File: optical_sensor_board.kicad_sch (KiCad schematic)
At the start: 18 parts, among them J2 Conn_01x09_Socket, U1 PMW3389DM‐T3QU, U3 LM317L_SOT-89

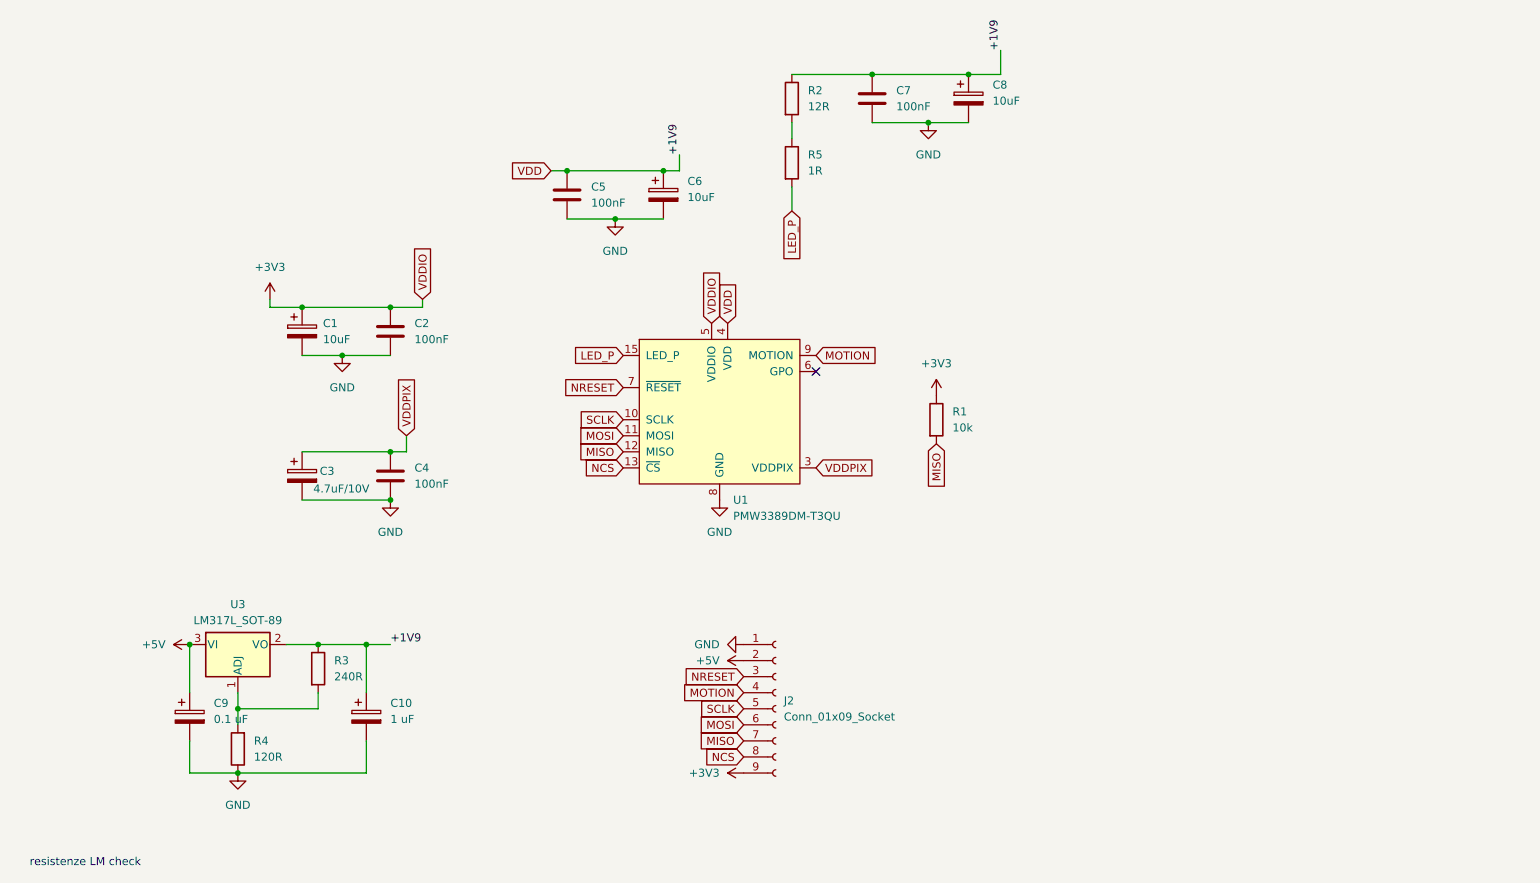
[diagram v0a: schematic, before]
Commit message: Aggiunta copper-area + modifiche a schematico e master
Design:
 - Spostate le tracce sul bottom e i ponti sul top layer
 - Aggiunta la Copper Area sul bottom layer
 - Sistemate le serigrafie

Schematico:
 - Corretti gli errori del ERC aggiungendo i PWR_FLAG
 - Spostati i componenti per far si che si veda almeno un pezzettino di filo

Progetto:
 - Aggiunta la libreria dei footprint
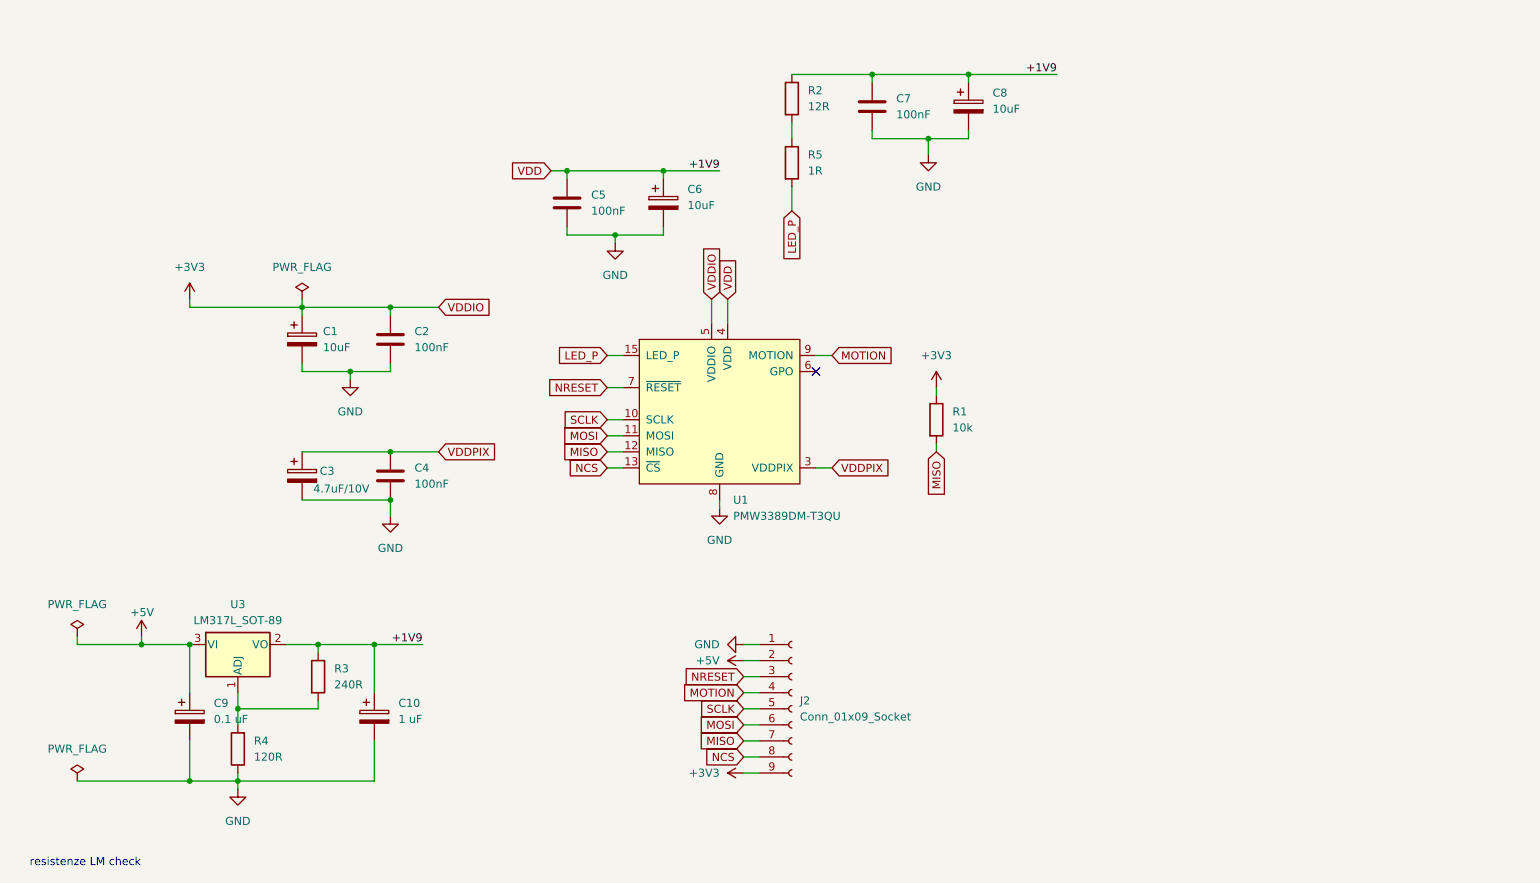
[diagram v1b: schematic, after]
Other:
- moved on the sheet: C1, C10, C2, C5, C6, C7, C8, J2, R3

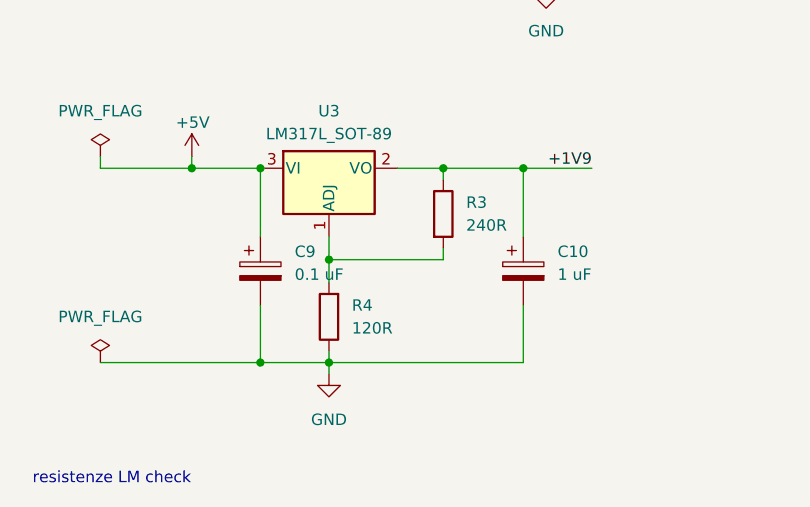
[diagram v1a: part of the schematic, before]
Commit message: add potentiometer in LM317 circuit
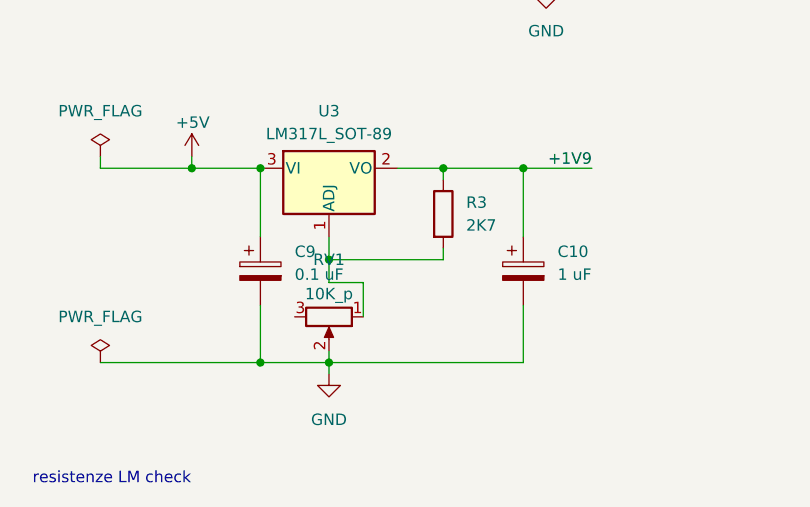
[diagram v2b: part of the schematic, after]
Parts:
- removed R4: 120R, MyOptical:LargePad_R_Axial_DIN0207_L6.3mm_D2.5mm_P10.16mm_Horizontal, symbol Device:R
- added RV1: 10K_p, symbol Device:R_Potentiometer
- R3: value 240R -> 2K7
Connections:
- net GND: now also RV1.2
- net at R3.2, U3.1 (ADJ): now also RV1.1
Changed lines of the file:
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@@
+	(wire
+		(pts
+			(xy 72.39 148.59) (xy 72.39 144.78)
+		)
+		(stroke
+			(width 0)
+			(type default)
+		)
+	)
 	(wire
 		(pts
@@
 		(pts
 			(xy 68.58 142.24) (xy 68.58 144.78)
+		)
+		(stroke
+			(width 0)
+			(type default)
+		)
+	)
+	(wire
+		(pts
+			(xy 72.39 144.78) (xy 68.58 144.78)
 		)
 		(stroke
@@
 	)
 	(symbol
+		(lib_id "Device:R_Potentiometer")
+		(at 68.58 148.59 270)
+		(unit 1)
+		(exclude_from_sim no)
+		(in_bom yes)
+		(on_board yes)
+		(dnp no)
+		(property "Reference" "RV1"
+			(at 68.58 142.24 90)
+			(effects
+				(font
+					(size 1.27 1.27)
+				)
+			)
+		)
+		(property "Value" "10K_p"
+			(at 68.58 146.05 90)
+			(effects
+				(font
+					(size 1.27 1.27)
+				)
+			)
+		)
+		(property "Footprint" ""
+			(at 68.58 148.59 0)
+			(effects
+				(font
+					(size 1.27 1.27)
+				)
+				(hide yes)
+			)
+		)
+		(property "Datasheet" "~"
+			(at 68.58 148.59 0)
+			(effects
+				(font
+					(size 1.27 1.27)
+				)
+				(hide yes)
+			)
+		)
+		(property "Description" "Potentiometer"
+			(at 68.58 148.59 0)
+			(effects
+				(font
+					(size 1.27 1.27)
+				)
+				(hide yes)
+			)
+		)
+		(pin "2"
+		)
+		(pin "1"
+		)
+		(pin "3"
+		)
+		(instances
+			(project ""
+				(path "/bc898632-37cb-47d1-8655-c4a22efc7ca2"
+					(reference "RV1")
+					(unit 1)
+				)
+			)
+		)
+	)
+	(symbol
 		(lib_id "power:GND")
 		(at 177.8 54.61 0)
@@
 				(path "/bc898632-37cb-47d1-8655-c4a22efc7ca2"
 					(reference "#PWR07")
-					(unit 1)
-				)
-			)
-		)
-	)
-	(symbol
-		(lib_id "Device:R")
-		(at 68.58 148.59 180)
-		(unit 1)
-		(exclude_from_sim no)
-		(in_bom yes)
-		(on_board yes)
-		(dnp no)
-		(fields_autoplaced yes)
-		(property "Reference" "R4"
-			(at 71.12 147.3199 0)
-			(effects
-				(font
-					(size 1.27 1.27)
-				)
-				(justify right)
-			)
-		)
-		(property "Value" "120R"
-			(at 71.12 149.8599 0)
-			(effects
-				(font
-					(size 1.27 1.27)
-				)
-				(justify right)
-			)
-		)
-		(property "Footprint" "MyOptical:LargePad_R_Axial_DIN0207_L6.3mm_D2.5mm_P10.16mm_Horizontal"
-			(at 70.358 148.59 90)
-			(effects
-				(font
-					(size 1.27 1.27)
-				)
-				(hide yes)
-			)
-		)
-		(property "Datasheet" "~"
-			(at 68.58 148.59 0)
-			(effects
-				(font
-					(size 1.27 1.27)
-				)
-				(hide yes)
-			)
-		)
-		(property "Description" "Resistor"
-			(at 68.58 148.59 0)
-			(effects
-				(font
-					(size 1.27 1.27)
-				)
-				(hide yes)
-			)
-		)
-		(pin "1"
-		)
-		(pin "2"
-		)
-		(instances
-			(project ""
-				(path "/bc898632-37cb-47d1-8655-c4a22efc7ca2"
-					(reference "R4")
 					(unit 1)
 				)
@@
 			)
 		)
-		(property "Value" "240R"
+		(property "Value" "2K7"
 			(at 83.82 138.4299 0)
 			(effects

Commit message: potentiometer footprint + potentiometer routing
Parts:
- RV1: footprint (none) -> MyOptical:LargerPad_P160
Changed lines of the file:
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@@
 			)
 		)
-		(property "Footprint" ""
+		(property "Footprint" "MyOptical:LargerPad_P160"
 			(at 68.58 148.59 0)
 			(effects

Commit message: copper area
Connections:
- no-connect marks 1 -> 2
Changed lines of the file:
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@@
+	)
+	(no_connect
+		(at 64.77 148.59)
 	)
 	(no_connect

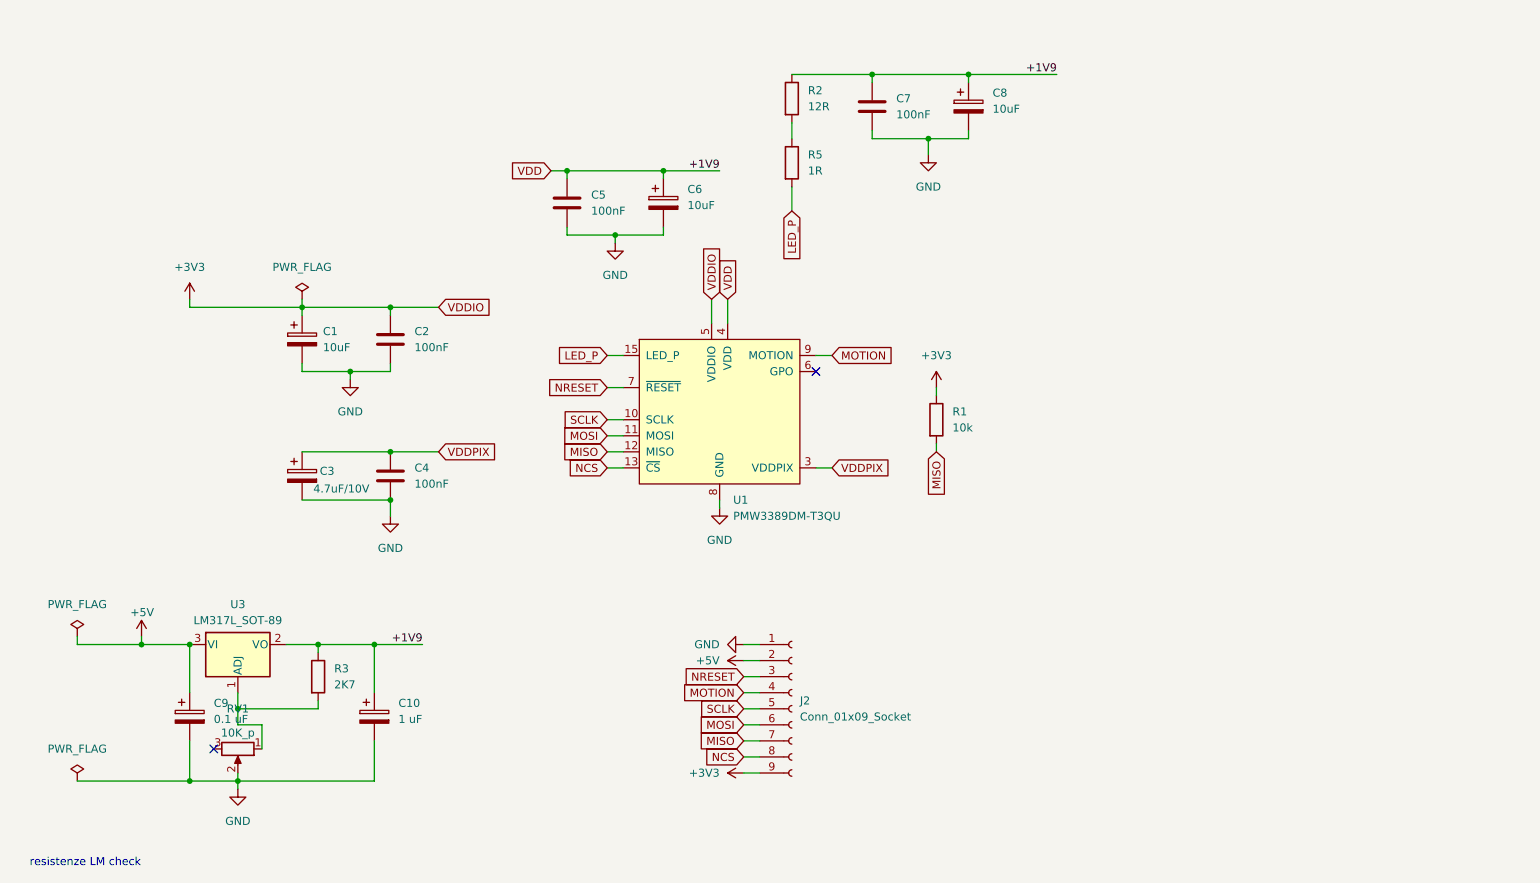
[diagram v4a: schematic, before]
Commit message: TestPoint in Schematic
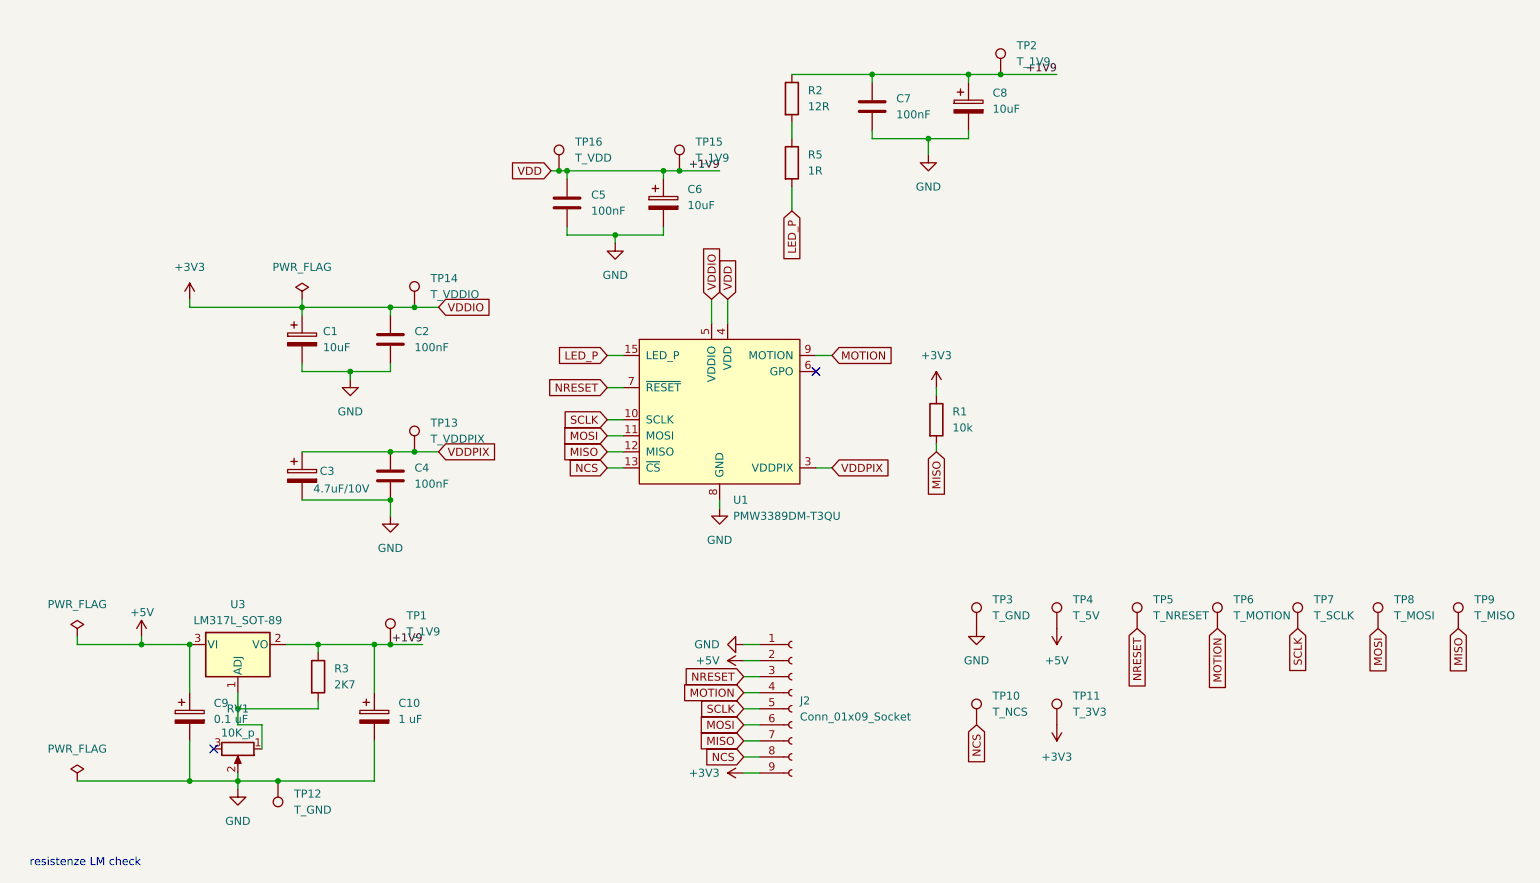
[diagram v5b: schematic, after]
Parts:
- added TP1, TP15, TP2: T_1V9, symbol Connector:TestPoint
- added TP10: T_NCS, symbol Connector:TestPoint
- added TP11: T_3V3, symbol Connector:TestPoint
- added TP12, TP3: T_GND, symbol Connector:TestPoint
- added TP13: T_VDDPIX, symbol Connector:TestPoint
- added TP14: T_VDDIO, symbol Connector:TestPoint
- added TP16: T_VDD, symbol Connector:TestPoint
- added TP4: T_5V, symbol Connector:TestPoint
- added TP5: T_NRESET, symbol Connector:TestPoint
- added TP6: T_MOTION, symbol Connector:TestPoint
- added TP7: T_SCLK, symbol Connector:TestPoint
- added TP8: T_MOSI, symbol Connector:TestPoint
- added TP9: T_MISO, symbol Connector:TestPoint
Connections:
- net +3V3: now also TP11.1, TP14.1
- net +5V: now also TP4.1
- net GND: now also TP12.1, TP3.1
- net MISO: now also TP9.1
- net MOSI: now also TP8.1
- net MOTION: now also TP6.1
- net NCS: now also TP10.1
- net NRESET: now also TP5.1
- net SCLK: now also TP7.1
- net VDD: now also TP1.1, TP15.1, TP16.1, TP2.1
- net VDDPIX: now also TP13.1

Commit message: add Footprint TestPoint
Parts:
- TP1, TP10, TP11, TP12, TP13, TP14, TP15, TP16, TP2, TP3, TP4, TP5, TP6, TP7, TP8, TP9: footprint (none) -> TestPoint:TestPoint_Keystone_5019_Miniature
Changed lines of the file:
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@@
 			)
 		)
-		(property "Footprint" ""
+		(property "Footprint" "TestPoint:TestPoint_Keystone_5019_Miniature"
 			(at 203.2 144.78 0)
 			(effects
@@
 			)
 		)
-		(property "Footprint" ""
+		(property "Footprint" "TestPoint:TestPoint_Keystone_5019_Miniature"
 			(at 101.6 101.6 0)
 			(effects
@@
 			)
 		)
-		(property "Footprint" ""
+		(property "Footprint" "TestPoint:TestPoint_Keystone_5019_Miniature"
 			(at 266.7 129.54 0)
 			(effects
@@
 			)
 		)
-		(property "Footprint" ""
+		(property "Footprint" "TestPoint:TestPoint_Keystone_5019_Miniature"
 			(at 101.6 78.74 0)
 			(effects
@@
 			)
 		)
-		(property "Footprint" ""
+		(property "Footprint" "TestPoint:TestPoint_Keystone_5019_Miniature"
 			(at 190.5 129.54 0)
 			(effects
@@
 			)
 		)
-		(property "Footprint" ""
+		(property "Footprint" "TestPoint:TestPoint_Keystone_5019_Miniature"
 			(at 254 129.54 0)
 			(effects
@@
 			)
 		)
-		(property "Footprint" ""
+		(property "Footprint" "TestPoint:TestPoint_Keystone_5019_Miniature"
 			(at 194.31 41.91 0)
 			(effects
@@
 			)
 		)
-		(property "Footprint" ""
+		(property "Footprint" "TestPoint:TestPoint_Keystone_5019_Miniature"
 			(at 215.9 129.54 0)
 			(effects
@@
 			)
 		)
-		(property "Footprint" ""
+		(property "Footprint" "TestPoint:TestPoint_Keystone_5019_Miniature"
 			(at 69.85 153.67 0)
 			(effects
@@
 			)
 		)
-		(property "Footprint" ""
+		(property "Footprint" "TestPoint:TestPoint_Keystone_5019_Miniature"
 			(at 190.5 144.78 0)
 			(effects
@@
 			)
 		)
-		(property "Footprint" ""
+		(property "Footprint" "TestPoint:TestPoint_Keystone_5019_Miniature"
 			(at 241.3 129.54 0)
 			(effects
@@
 			)
 		)
-		(property "Footprint" ""
+		(property "Footprint" "TestPoint:TestPoint_Keystone_5019_Miniature"
 			(at 124.46 57.15 0)
 			(effects
@@
 			)
 		)
-		(property "Footprint" ""
+		(property "Footprint" "TestPoint:TestPoint_Keystone_5019_Miniature"
 			(at 228.6 129.54 0)
 			(effects
@@
 			)
 		)
-		(property "Footprint" ""
+		(property "Footprint" "TestPoint:TestPoint_Keystone_5019_Miniature"
 			(at 143.51 57.15 0)
 			(effects
@@
 			)
 		)
-		(property "Footprint" ""
+		(property "Footprint" "TestPoint:TestPoint_Keystone_5019_Miniature"
 			(at 203.2 129.54 0)
 			(effects
@@
 			)
 		)
-		(property "Footprint" ""
+		(property "Footprint" "TestPoint:TestPoint_Keystone_5019_Miniature"
 			(at 97.79 132.08 0)
 			(effects
